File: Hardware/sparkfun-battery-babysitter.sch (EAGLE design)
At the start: 56 parts, among them U1 BQ24075, U2 BQ27441-G1

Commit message: Adding a few PROD_ID's
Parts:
- R7: PROD_ID (none) -> TBD
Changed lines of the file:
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@@
 <grid distance="0.1" unitdist="inch" unit="inch" style="lines" multiple="1" display="no" altdistance="0.01" altunitdist="inch" altunit="inch"/>
 <layers>
-<layer number="1" name="Top" color="4" fill="1" visible="yes" active="no"/>
-<layer number="2" name="Route2" color="1" fill="3" visible="yes" active="no"/>
-<layer number="3" name="Route3" color="4" fill="3" visible="yes" active="no"/>
-<layer number="4" name="Route4" color="1" fill="4" visible="yes" active="no"/>
-<layer number="5" name="Route5" color="4" fill="4" visible="yes" active="no"/>
-<layer number="6" name="Route6" color="1" fill="8" visible="yes" active="no"/>
-<layer number="7" name="Route7" color="4" fill="8" visible="yes" active="no"/>
-<layer number="8" name="Route8" color="1" fill="2" visible="yes" active="no"/>
-<layer number="9" name="Route9" color="4" fill="2" visible="yes" active="no"/>
-<layer number="10" name="Route10" color="1" fill="7" visible="yes" active="no"/>
-<layer number="11" name="Route11" color="4" fill="7" visible="yes" active="no"/>
-<layer number="12" name="Route12" color="1" fill="5" visible="yes" active="no"/>
-<layer number="13" name="Route13" color="4" fill="5" visible="yes" active="no"/>
-<layer number="14" name="Route14" color="1" fill="6" visible="yes" active="no"/>
-<layer number="15" name="Route15" color="4" fill="6" visible="yes" active="no"/>
-<layer number="16" name="Bottom" color="1" fill="1" visible="yes" active="no"/>
-<layer number="17" name="Pads" color="2" fill="1" visible="yes" active="no"/>
-<layer number="18" name="Vias" color="2" fill="1" visible="yes" active="no"/>
-<layer number="19" name="Unrouted" color="6" fill="1" visible="yes" active="no"/>
-<layer number="20" name="Dimension" color="15" fill="1" visible="yes" active="no"/>
-<layer number="21" name="tPlace" color="16" fill="1" visible="yes" active="no"/>
-<layer number="22" name="bPlace" color="14" fill="1" visible="yes" active="no"/>
-<layer number="23" name="tOrigins" color="15" fill="1" visible="yes" active="no"/>
-<layer number="24" name="bOrigins" color="15" fill="1" visible="yes" active="no"/>
-<layer number="25" name="tNames" color="7" fill="1" visible="yes" active="no"/>
-<layer number="26" name="bNames" color="7" fill="1" visible="yes" active="no"/>
-<layer number="27" name="tValues" color="7" fill="1" visible="yes" active="no"/>
-<layer number="28" name="bValues" color="7" fill="1" visible="yes" active="no"/>
+<layer number="1" name="Top" color="4" fill="1" visible="no" active="no"/>
+<layer number="2" name="Route2" color="1" fill="3" visible="no" active="no"/>
+<layer number="3" name="Route3" color="4" fill="3" visible="no" active="no"/>
+<layer number="4" name="Route4" color="1" fill="4" visible="no" active="no"/>
+<layer number="5" name="Route5" color="4" fill="4" visible="no" active="no"/>
+<layer number="6" name="Route6" color="1" fill="8" visible="no" active="no"/>
+<layer number="7" name="Route7" color="4" fill="8" visible="no" active="no"/>
+<layer number="8" name="Route8" color="1" fill="2" visible="no" active="no"/>
+<layer number="9" name="Route9" color="4" fill="2" visible="no" active="no"/>
+<layer number="10" name="Route10" color="1" fill="7" visible="no" active="no"/>
+<layer number="11" name="Route11" color="4" fill="7" visible="no" active="no"/>
+<layer number="12" name="Route12" color="1" fill="5" visible="no" active="no"/>
+<layer number="13" name="Route13" color="4" fill="5" visible="no" active="no"/>
+<layer number="14" name="Route14" color="1" fill="6" visible="no" active="no"/>
+<layer number="15" name="Route15" color="4" fill="6" visible="no" active="no"/>
+<layer number="16" name="Bottom" color="1" fill="1" visible="no" active="no"/>
+<layer number="17" name="Pads" color="2" fill="1" visible="no" active="no"/>
+<layer number="18" name="Vias" color="2" fill="1" visible="no" active="no"/>
+<layer number="19" name="Unrouted" color="6" fill="1" visible="no" active="no"/>
+<layer number="20" name="Dimension" color="15" fill="1" visible="no" active="no"/>
+<layer number="21" name="tPlace" color="16" fill="1" visible="no" active="no"/>
+<layer number="22" name="bPlace" color="14" fill="1" visible="no" active="no"/>
+<layer number="23" name="tOrigins" color="15" fill="1" visible="no" active="no"/>
+<layer number="24" name="bOrigins" color="15" fill="1" visible="no" active="no"/>
+<layer number="25" name="tNames" color="7" fill="1" visible="no" active="no"/>
+<layer number="26" name="bNames" color="7" fill="1" visible="no" active="no"/>
+<layer number="27" name="tValues" color="7" fill="1" visible="no" active="no"/>
+<layer number="28" name="bValues" color="7" fill="1" visible="no" active="no"/>
 <layer number="29" name="tStop" color="7" fill="3" visible="no" active="no"/>
 <layer number="30" name="bStop" color="7" fill="6" visible="no" active="no"/>
@@
 <layer number="35" name="tGlue" color="7" fill="4" visible="no" active="no"/>
 <layer number="36" name="bGlue" color="7" fill="5" visible="no" active="no"/>
-<layer number="37" name="tTest" color="7" fill="1" visible="yes" active="no"/>
-<layer number="38" name="bTest" color="7" fill="1" visible="yes" active="no"/>
+<layer number="37" name="tTest" color="7" fill="1" visible="no" active="no"/>
+<layer number="38" name="bTest" color="7" fill="1" visible="no" active="no"/>
 <layer number="39" name="tKeepout" color="4" fill="11" visible="no" active="no"/>
 <layer number="40" name="bKeepout" color="1" fill="11" visible="no" active="no"/>
@@
 <layer number="44" name="Drills" color="7" fill="1" visible="no" active="no"/>
 <layer number="45" name="Holes" color="7" fill="1" visible="no" active="no"/>
-<layer number="46" name="Milling" color="3" fill="1" visible="yes" active="no"/>
-<layer number="47" name="Measures" color="7" fill="1" visible="yes" active="no"/>
-<layer number="48" name="Document" color="7" fill="1" visible="yes" active="no"/>
-<layer number="49" name="Reference" color="7" fill="1" visible="yes" active="no"/>
-<layer number="50" name="dxf" color="7" fill="1" visible="yes" active="no"/>
-<layer number="51" name="tDocu" color="6" fill="1" visible="yes" active="no"/>
-<layer number="52" name="bDocu" color="7" fill="1" visible="yes" active="no"/>
-<layer number="53" name="tGND_GNDA" color="7" fill="9" visible="yes" active="no"/>
-<layer number="54" name="bGND_GNDA" color="1" fill="9" visible="yes" active="no"/>
-<layer number="56" name="wert" color="7" fill="1" visible="yes" active="no"/>
-<layer number="57" name="tCAD" color="7" fill="1" visible="yes" active="no"/>
-<layer number="59" name="tCarbon" color="7" fill="1" visible="yes" active="no"/>
-<layer number="60" name="bCarbon" color="7" fill="1" visible="yes" active="no"/>
+<layer number="46" name="Milling" color="3" fill="1" visible="no" active="no"/>
+<layer number="47" name="Measures" color="7" fill="1" visible="no" active="no"/>
+<layer number="48" name="Document" color="7" fill="1" visible="no" active="no"/>
+<layer number="49" name="Reference" color="7" fill="1" visible="no" active="no"/>
+<layer number="50" name="dxf" color="7" fill="1" visible="no" active="no"/>
+<layer number="51" name="tDocu" color="6" fill="1" visible="no" active="no"/>
+<layer number="52" name="bDocu" color="7" fill="1" visible="no" active="no"/>
+<layer number="53" name="tGND_GNDA" color="7" fill="9" visible="no" active="no"/>
+<layer number="54" name="bGND_GNDA" color="1" fill="9" visible="no" active="no"/>
+<layer number="56" name="wert" color="7" fill="1" visible="no" active="no"/>
+<layer number="57" name="tCAD" color="7" fill="1" visible="no" active="no"/>
+<layer number="59" name="tCarbon" color="7" fill="1" visible="no" active="no"/>
+<layer number="60" name="bCarbon" color="7" fill="1" visible="no" active="no"/>
 <layer number="90" name="Modules" color="5" fill="1" visible="yes" active="yes"/>
 <layer number="91" name="Nets" color="2" fill="1" visible="yes" active="yes"/>
@@
 <attribute name="PROD_ID" value="TBD"/>
 </part>
-<part name="R7" library="SparkFun-Passives" deviceset="RESISTOR" device="0603-RES" value="1.1k"/>
+<part name="R7" library="SparkFun-Passives" deviceset="RESISTOR" device="0603-RES" value="1.1k">
+<attribute name="PROD_ID" value="TBD"/>
+</part>
 <part name="GND6" library="SparkFun-Aesthetics" deviceset="GND" device=""/>
 <part name="GND9" library="SparkFun-Aesthetics" deviceset="GND" device=""/>
@@
 <attribute name="NAME" x="59.9186" y="59.69" size="1.778" layer="95" rot="R270"/>
 <attribute name="VALUE" x="59.944" y="54.61" size="1.778" layer="96" rot="R270"/>
+<attribute name="PROD_ID" x="58.42" y="55.88" size="1.27" layer="96" rot="R270" display="off"/>
 </instance>
 <instance part="GND6" gate="1" x="43.18" y="48.26"/>

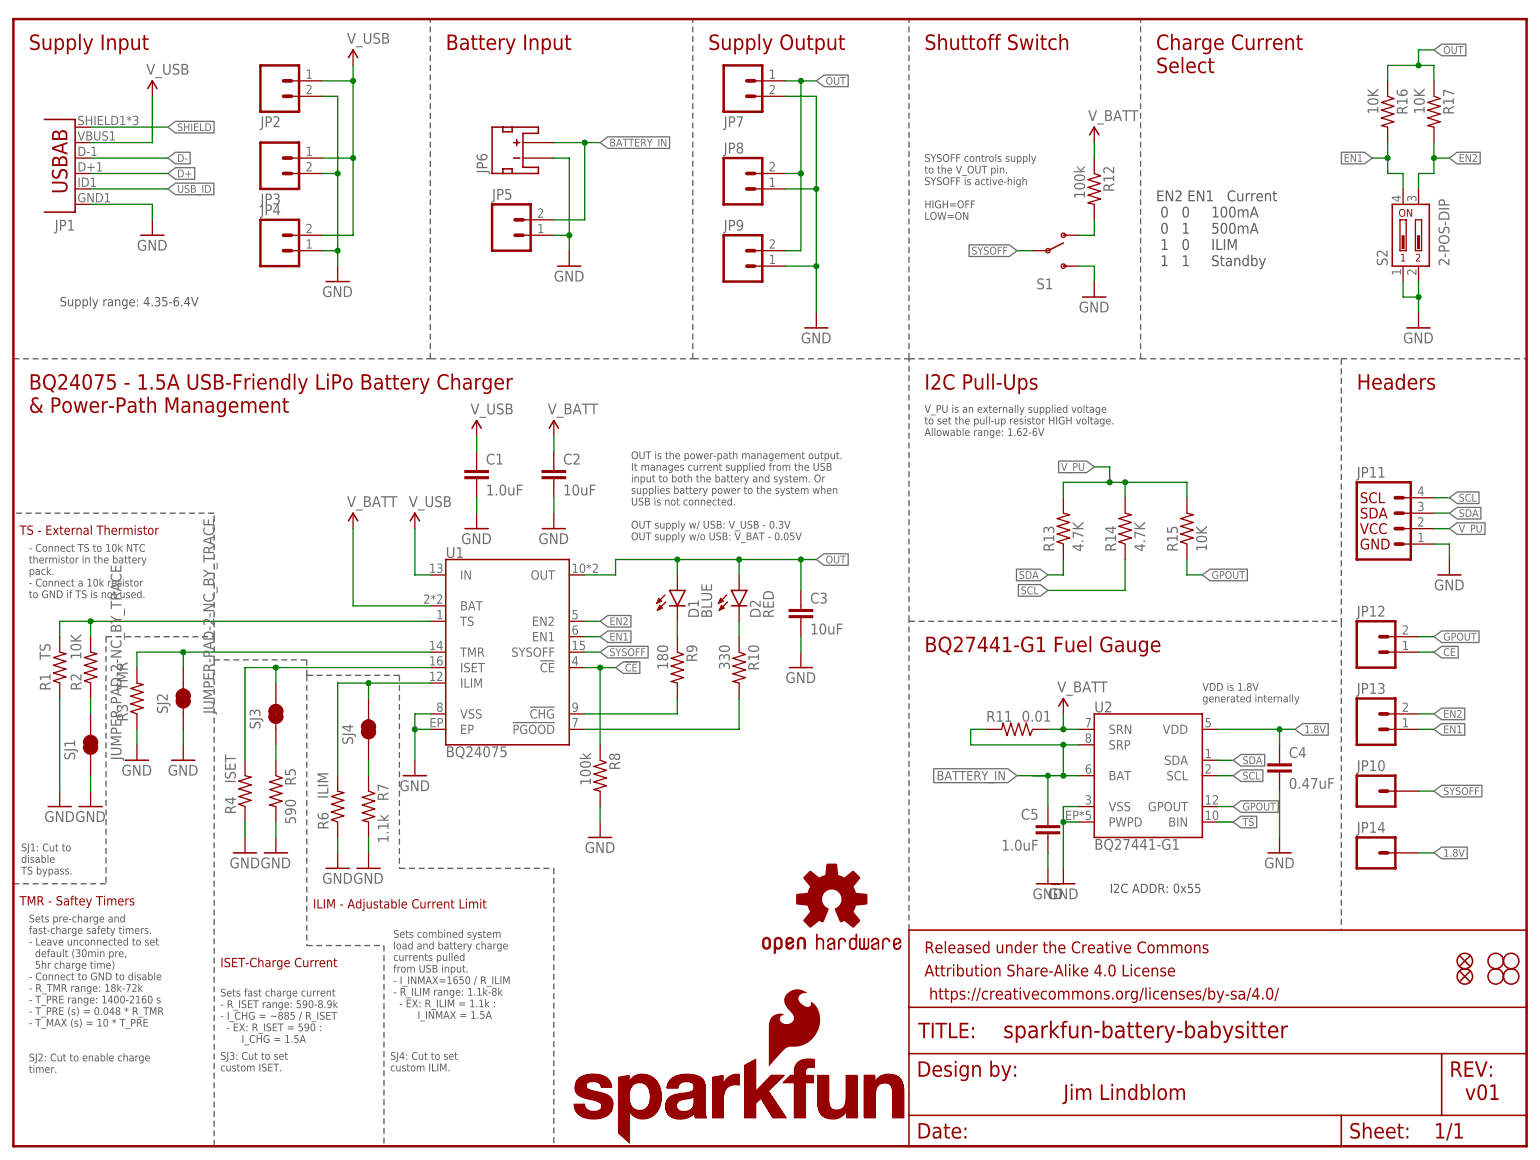
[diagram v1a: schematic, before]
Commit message: Swapping out DIP switch for larger variant
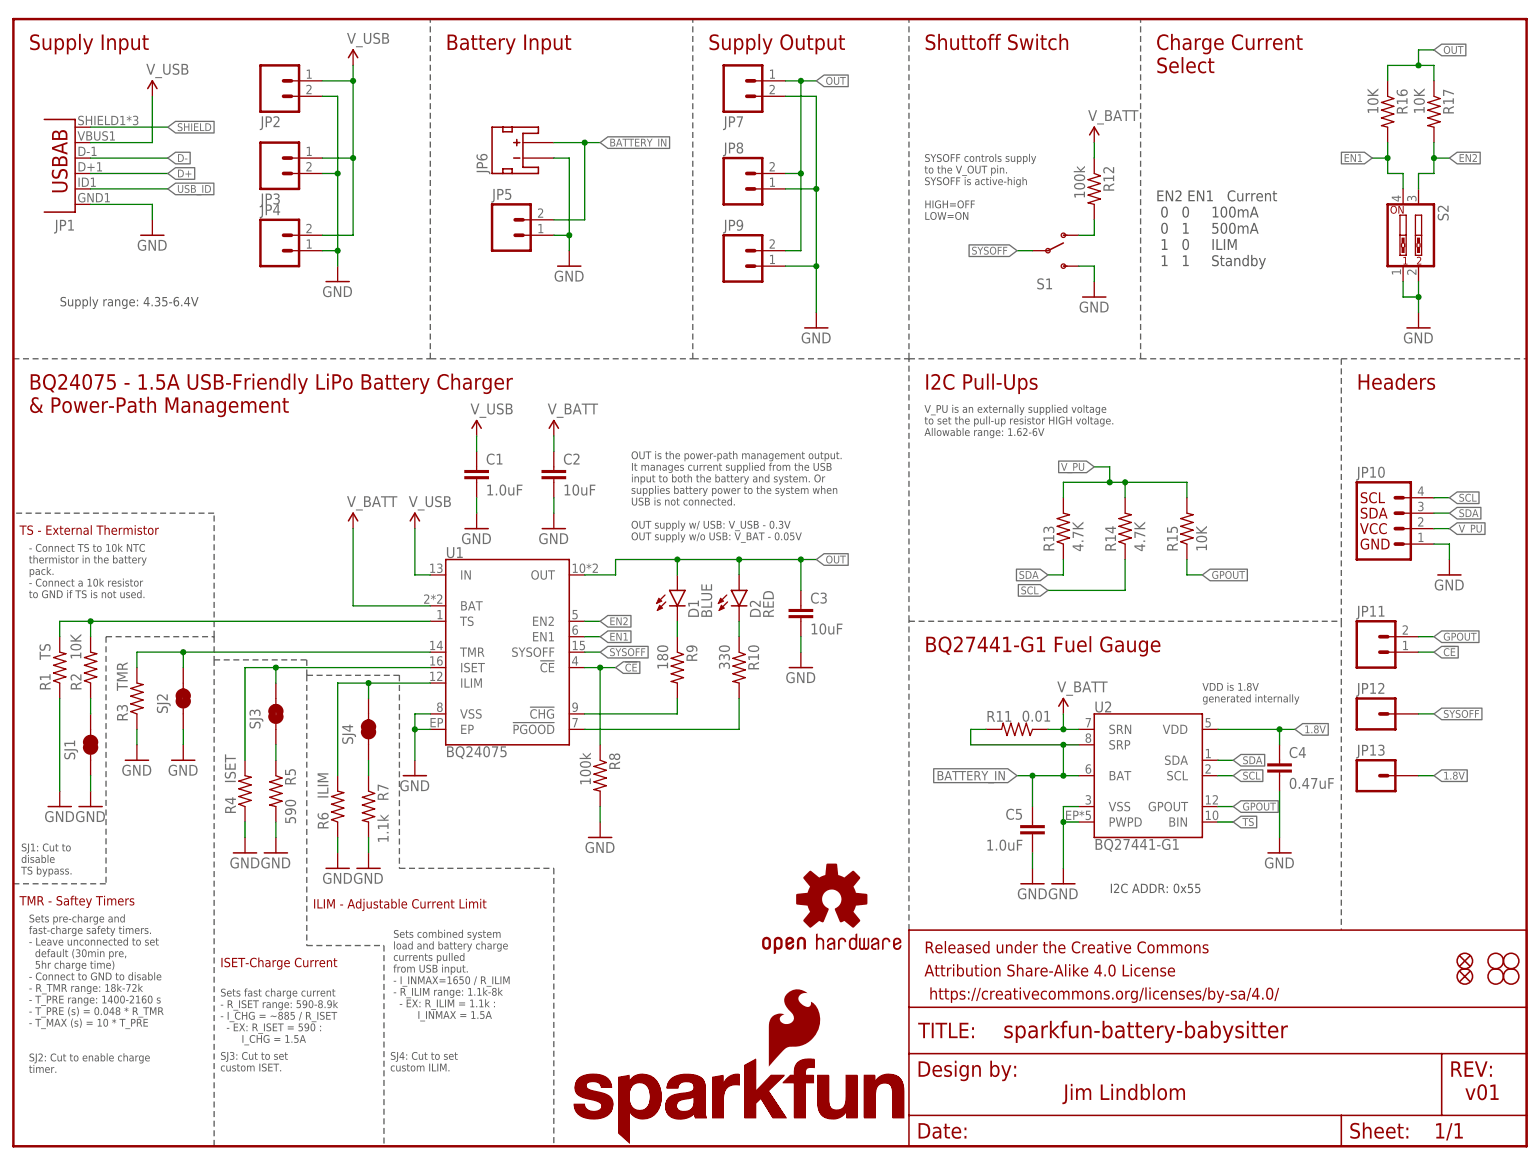
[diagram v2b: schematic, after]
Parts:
- removed JP14: (no value), SparkFun-Connectors:M01PTH_NO_SILK_YES_STOP
- JP10: device SparkFun-Connectors:M01PTH_NO_SILK_YES_STOP -> SparkFun-Connectors:I2C_STANDARD_NO_SILK
- JP11: device SparkFun-Connectors:I2C_STANDARD_NO_SILK -> SparkFun-Connectors:M021X02_NO_SILK
- JP12, JP13: device SparkFun-Connectors:M021X02_NO_SILK -> SparkFun-Connectors:M01PTH_NO_SILK_YES_STOP
- S2: value 2-POS-DIP -> (none); device SparkFun-Electromechanical:2-POS-DIP -> SparkFun-Electromechanical:SW_DIP-2-SMT-HALFSIZE; PROD_ID (none) -> TBD
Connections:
- net !CE!: now also JP11.1; no longer JP12.1
- net 1.8V: now also JP13.1; no longer JP14.1
- net EN1: now also S2.4; no longer JP13.1, S2.P$4
- net EN2: now also S2.3; no longer JP13.2, S2.P$3
- net GND: now also JP10.1, S2.1, S2.2; no longer JP11.1, S2.P$1, S2.P$2
- net GPOUT: now also JP11.2; no longer JP12.2
- net SCL: now also JP10.4; no longer JP11.4
- net SDA: now also JP10.3; no longer JP11.3
- net SYSOFF: now also JP12.1; no longer JP10.1
- net V_PU: now also JP10.2; no longer JP11.2
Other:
- moved on the sheet: C5

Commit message: Nudging sparkfun logo
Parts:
- S2: PROD_ID TBD -> SWCH-13215
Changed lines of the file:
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@@
 <part name="FID2" library="SparkFun-Aesthetics" deviceset="FIDUCIAL" device="1X2"/>
 <part name="S2" library="SparkFun-Electromechanical" deviceset="SW_DIP-2" device="-SMT-HALFSIZE">
-<attribute name="PROD_ID" value="TBD"/>
+<attribute name="PROD_ID" value="SWCH-13215"/>
 </part>
 </parts>

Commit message: Adding PROD_ID's for new components
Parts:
- C4: PROD_ID TBD -> CAP-13216
- R11: PROD_ID TBD -> RES-13218
- R5: PROD_ID TBD -> RES-13217
- R7: PROD_ID TBD -> RES-10447
- U1: PROD_ID TBD -> IC-13219
- U2: PROD_ID TBD -> IC-13220
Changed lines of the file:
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@@
 <part name="SUPPLY1" library="SparkFun-Aesthetics" deviceset="V_USB" device=""/>
 <part name="U2" library="battery-management-temp" deviceset="BQ27441-G1" device="">
-<attribute name="PROD_ID" value="TBD"/>
+<attribute name="PROD_ID" value="IC-13220"/>
 </part>
 <part name="R11" library="SparkFun-Resistors" deviceset="RESISTOR" device="1206" value="0.01">
-<attribute name="PROD_ID" value="TBD"/>
+<attribute name="PROD_ID" value="RES-13218"/>
 </part>
 <part name="SUPPLY7" library="SparkFun-Aesthetics" deviceset="V_BATT" device=""/>
@@
 <part name="GND20" library="SparkFun-Aesthetics" deviceset="GND" device=""/>
 <part name="C4" library="SparkFun-Capacitors" deviceset="CAP" device="0603-CAP" value="0.47uF">
-<attribute name="PROD_ID" value="TBD"/>
+<attribute name="PROD_ID" value="CAP-13216"/>
 </part>
 <part name="GND19" library="SparkFun-Aesthetics" deviceset="GND" device=""/>
@@
 <part name="R14" library="SparkFun-Resistors" deviceset="4.7KOHM-1/10W-1%(0603)" device="" value="4.7K"/>
 <part name="U1" library="battery-management-temp" deviceset="BQ24075" device="">
-<attribute name="PROD_ID" value="TBD"/>
+<attribute name="PROD_ID" value="IC-13219"/>
 </part>
 <part name="GND10" library="SparkFun-Aesthetics" deviceset="GND" device=""/>
@@
 <part name="SUPPLY4" library="SparkFun-Aesthetics" deviceset="V_USB" device=""/>
 <part name="R5" library="SparkFun-Passives" deviceset="RESISTOR" device="0603-RES" value="590">
-<attribute name="PROD_ID" value="TBD"/>
+<attribute name="PROD_ID" value="RES-13217"/>
 </part>
 <part name="R7" library="SparkFun-Passives" deviceset="RESISTOR" device="0603-RES" value="1.1k">
-<attribute name="PROD_ID" value="TBD"/>
+<attribute name="PROD_ID" value="RES-10447"/>
 </part>
 <part name="GND6" library="SparkFun-Aesthetics" deviceset="GND" device=""/>
